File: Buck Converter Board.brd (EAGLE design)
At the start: 120.6 x 47.7 mm, 8 parts, among them J1 POWERPOLE_POWER25A_HORIZONTAL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, J2 POWERPOLE_POWER25A_HORIZONTAL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, J3 POWERPOLE_POWER25A_HORIZONTAL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

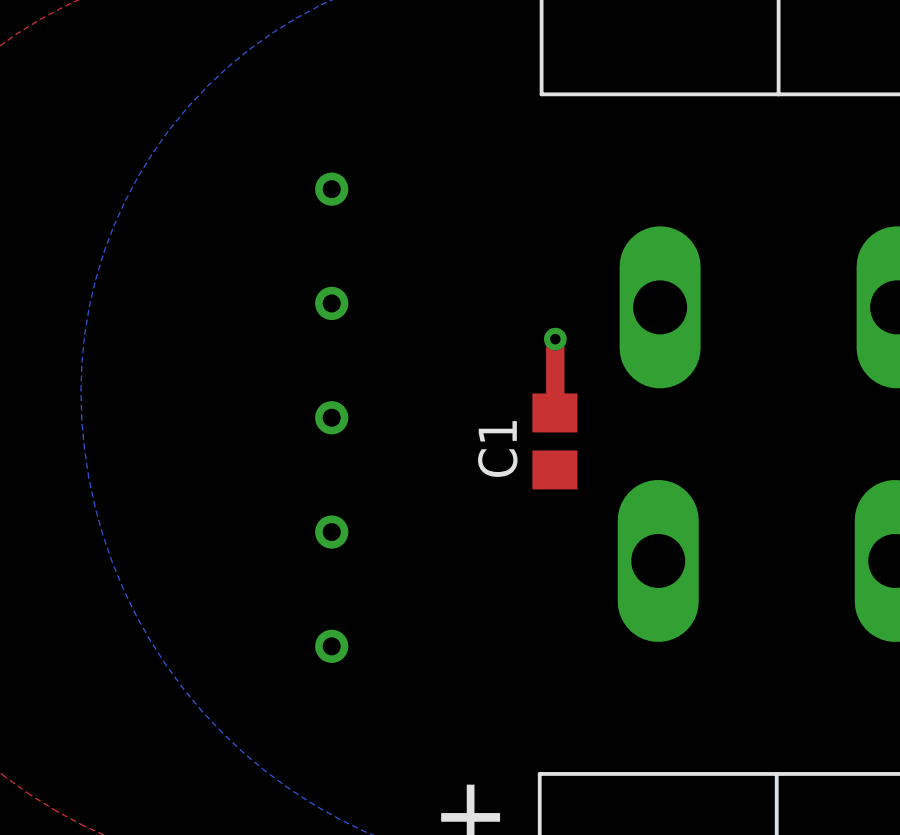
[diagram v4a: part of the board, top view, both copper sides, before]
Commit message: connected sense pins on buck board
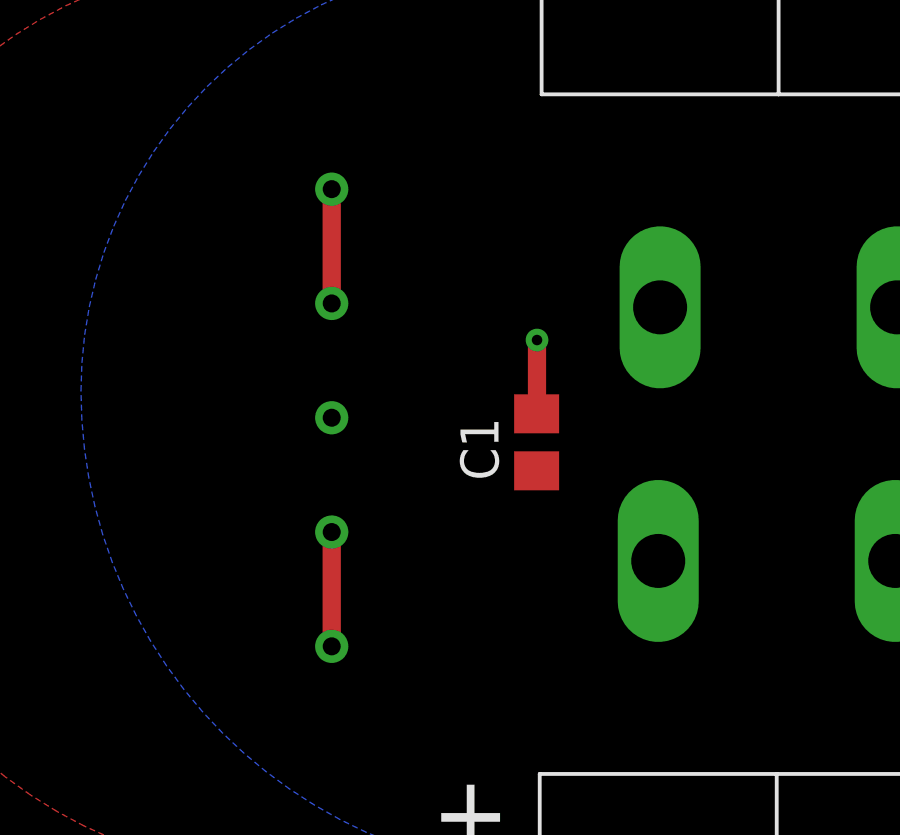
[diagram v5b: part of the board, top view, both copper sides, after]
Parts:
- C1: value (none) -> .47uF
- moved C1 0.61 mm to (96.0, 22.0)
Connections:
- net OGND: now also UEE150W.SNS-
- net V_OUT: now also UEE150W.SNS+
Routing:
- net OGND: track 2.47 -> 6.28 mm
- net V_OUT: track 0.00 -> 3.81 mm
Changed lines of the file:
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@@
 </autorouter>
 <elements>
-<element name="C1" library="rcl" library_urn="urn:adsk.eagle:library:334" package="C0805" package3d_urn="urn:adsk.eagle:package:23617/2" value="" x="96.62" y="22.06" smashed="yes" rot="R90">
-<attribute name="NAME" x="95.35" y="20.79" size="1.27" layer="25" rot="R90"/>
-<attribute name="SPICEPREFIX" value="C" x="96.62" y="22.06" size="1.778" layer="27" rot="R90" display="off"/>
-<attribute name="VALUE" x="99.16" y="20.79" size="1.27" layer="27" rot="R90"/>
+<element name="C1" library="rcl" library_urn="urn:adsk.eagle:library:334" package="C0805" package3d_urn="urn:adsk.eagle:package:23617/2" value=".47uF" x="96.01" y="22.03" smashed="yes" rot="R90">
+<attribute name="NAME" x="94.74" y="20.76" size="1.27" layer="25" rot="R90"/>
+<attribute name="SPICEPREFIX" value="C" x="96.01" y="22.03" size="1.778" layer="27" rot="R90" display="off"/>
+<attribute name="VALUE" x="98.55" y="20.76" size="1.27" layer="27" rot="R90"/>
 </element>
 <element name="F1" library="fuse" library_urn="urn:adsk.eagle:library:233" package="FUSE_HOLDER_5X20MM" package3d_urn="urn:adsk.eagle:package:14079/1" value="FUSEBLANK_5X20MM" x="14.58875" y="39.1875" smashed="yes">
@@
 </polygon>
 <contactref element="D2" pad="C"/>
+<contactref element="UEE150W" pad="SNS+"/>
+<wire x1="89.18" y1="26.66" x2="89.18" y2="30.47" width="0.6096" layer="1"/>
 </signal>
 <signal name="OGND" airwireshidden="yes">
@@
 </polygon>
 <contactref element="D2" pad="A"/>
-<wire x1="96.62" y1="23.01" x2="96.63375" y2="23.02375" width="0.6096" layer="1"/>
-<wire x1="96.63375" y1="23.02375" x2="96.63375" y2="25.47" width="0.6096" layer="1"/>
-<via x="96.63375" y="25.47" extent="1-16" drill="0.35"/>
+<wire x1="96.01" y1="22.98" x2="96.02375" y2="22.99375" width="0.6096" layer="1"/>
+<wire x1="96.02375" y1="22.99375" x2="96.02375" y2="25.44" width="0.6096" layer="1"/>
+<via x="96.02375" y="25.44" extent="1-16" drill="0.35"/>
+<contactref element="UEE150W" pad="SNS-"/>
+<wire x1="89.18" y1="19.04" x2="89.18" y2="15.23" width="0.6096" layer="1"/>
 </signal>
 </signals>
